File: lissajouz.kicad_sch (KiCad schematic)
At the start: 67 parts, among them J1 Conn_01x02_Male, J2 Conn_02x02_Odd_Even, Q1 2N7000, Q2 2N7000, Q3 2N7000, Q4 2N7000, Q5 2N7000, Q6 BC327, Q7 BC557, Q8 BC327, Q9 BC557, U1 LM324, U2 LM324, U3 LM324, U4 LM324, U5 TL074

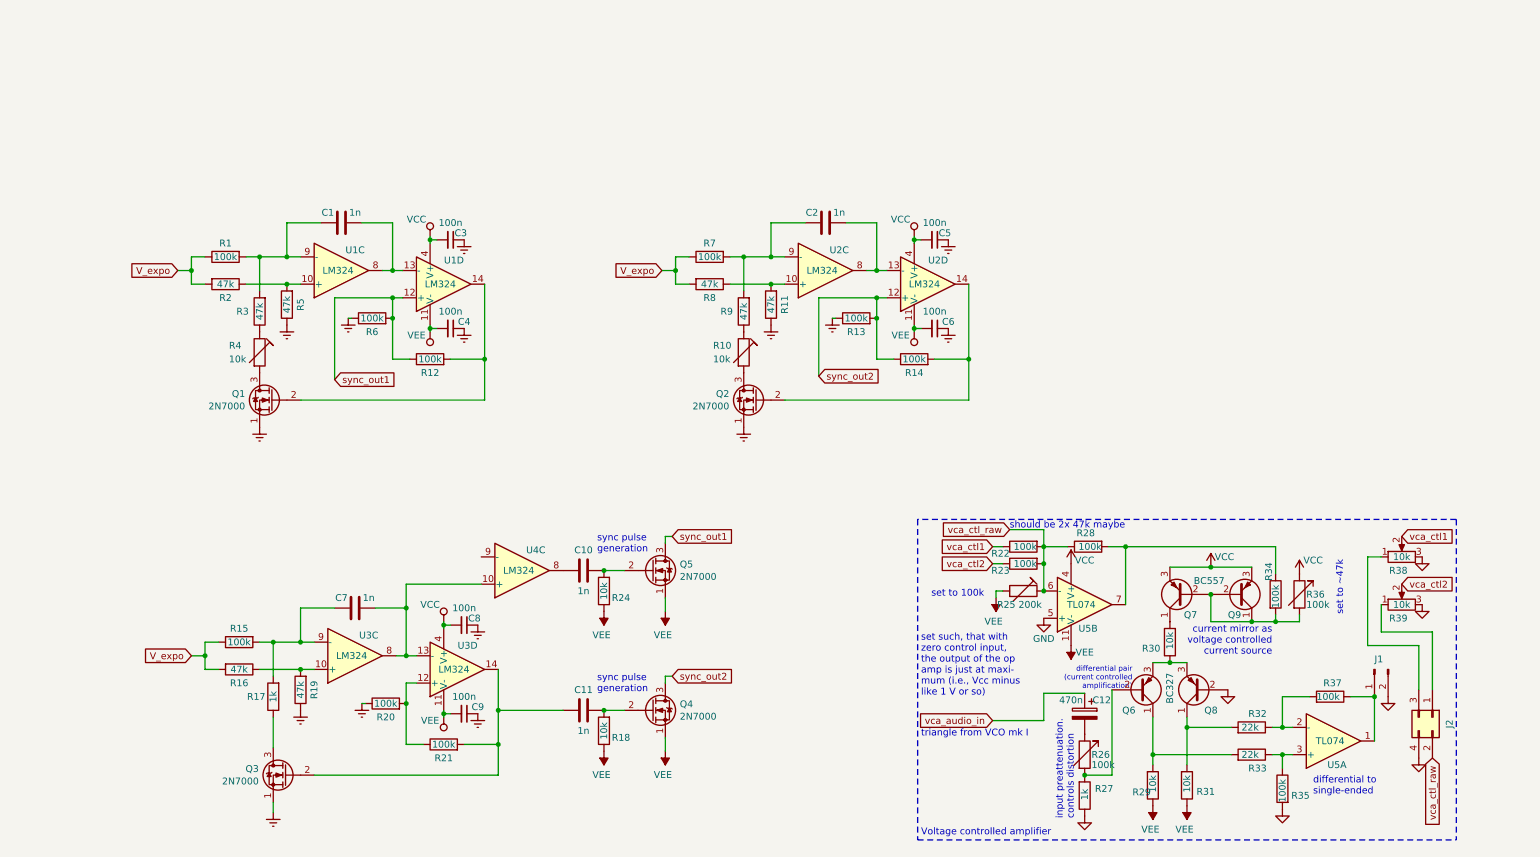
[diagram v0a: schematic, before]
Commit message: tried simulation, does not work
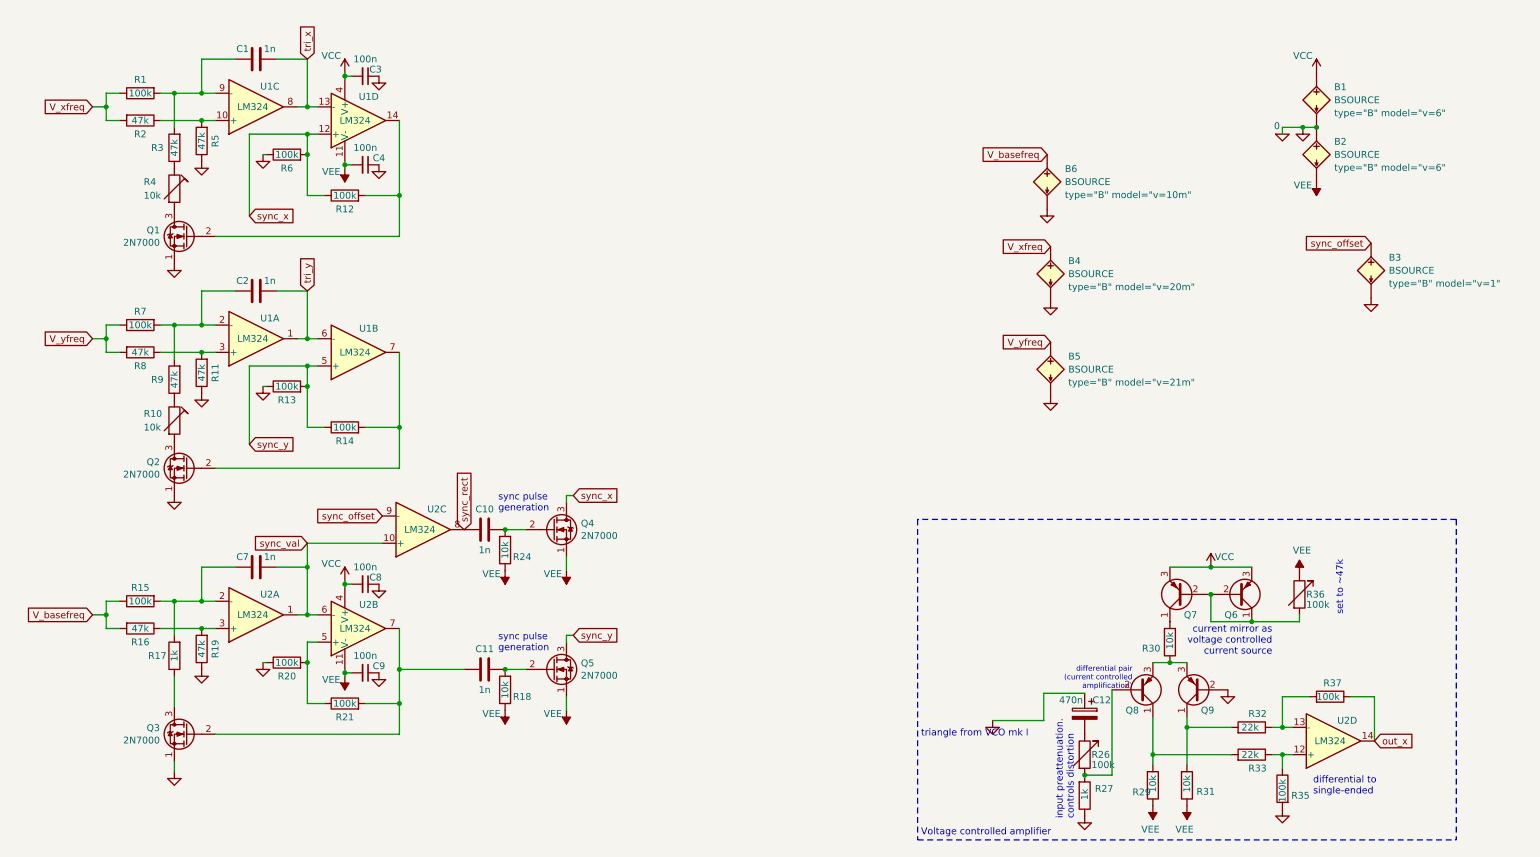
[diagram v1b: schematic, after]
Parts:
- removed C5, C6: 100n, Capacitor_SMD:C_0805_2012Metric_Pad1.15x1.40mm_HandSolder, symbol Device:C_Small
- removed J1: Conn_01x02_Male, Connector_PinHeader_2.54mm:PinHeader_1x02_P2.54mm_Vertical, symbol voice_board-rescue:Conn_01x02_Male-Connector
- removed J2: Conn_02x02_Odd_Even, Connector_PinHeader_2.54mm:PinHeader_2x02_P2.54mm_Vertical, symbol Connector_Generic:Conn_02x02_Odd_Even
- removed Q6, Q8: BC327, Package_TO_SOT_THT:TO-92_Inline, symbol Transistor_BJT:BC327
- removed R22, R23, R28, R34: 100k, Resistor_SMD:R_0805_2012Metric_Pad1.15x1.40mm_HandSolder, symbol Device:R
- removed R25: 200k, Potentiometer_THT:Potentiometer_Runtron_RM-065_Vertical, symbol voice_board-rescue:RTRIM-Device
- removed R38, R39: 10k, Potentiometer_THT:Potentiometer_Runtron_RM-065_Vertical, symbol voice_board-rescue:R_POT-Device
- removed unit 5 of U2
- removed U5: TL074, Package_DIP:DIP-14_W7.62mm, symbol Amplifier_Operational:TL074
- added B1, B2, B3, B4, B5, B6: BSOURCE, symbol Simulation_SPICE:BSOURCE
- added Q6, Q8: BC557, Package_TO_SOT_THT:TO-92_Inline, symbol Transistor_BJT:BC557
- added unit 4 of U2
- renumbered U2 to U1, U3 to U2, U4 to U2
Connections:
- net vca_audio_in is gone; now on net GND: C12.1
- net GND: now also Q9.2 (B)
- net VCC: now also B1.1 (N+), Q6.3 (E); no longer Q9.3 (E), R36.1
- net VEE: now also R36.1, B2.2 (N-)
- net at C11.1, R18.2: now also Q5.2 (G); no longer Q4.2 (G)
- net out_x: now reaches R37.1
- net out_x: now also U2.14
- net at Q7.2 (B), R36.2: now also Q6.1 (C), Q6.2 (B); no longer Q9.1 (C), Q9.2 (B)
- net at C2.2, R7.2, R9.2: now also U1.2 (-); no longer U1.9 (-)
- net at R20.2, R21.1: now also U2.5 (+); no longer U2.12 (+)
- net sync_val: now reaches C7.1, U2.10 (+)
- net sync_val: now also U2.1, U2.6 (-); no longer U2.13 (-), U2.8
- net at C11.2, Q3.2 (G), R21.2: now also U2.7; no longer U2.14
- net at R33.1, R35.1: now also U2.12 (+)
- net at R11.2, R8.1: now also U1.3 (+); no longer U1.10 (+)
- net at R29.2, R33.2: now also Q8.1 (C)
- net at R16.1, R19.2: now also U2.3 (+); no longer U2.10 (+)
- net at C7.2, R15.2, R17.2: now also U2.2 (-); no longer U2.9 (-)
- net at Q2.2 (G), R14.2: now also U1.7; no longer U1.14
- net at C10.1, R24.2: now also Q4.2 (G); no longer Q5.2 (G)
- net sync_rect: now reaches C10.2, U2.8
- net sync_offset: now reaches U2.9 (-)
- net sync_offset: now also B3.1 (N+)
- net at R26.2, R27.2: now also Q8.2 (B)
- net at R30.1: now also Q9.3 (E), Q8.3 (E)
- net at R32.1, R37.2: now also U2.13 (-)
- net at R31.2, R32.2: now also Q9.1 (C)
- net tri_x: now reaches C1.1, U1.13 (-), U1.8
- net GNDREF renamed 0
- net 0: now also B1.2 (N-), B2.1 (N+), B3.2 (N-), B4.2 (N-), B5.2 (N-), B6.2 (N-)
- removed net V_expo: R1.1, R15.1, R16.2, R2.2, R7.1, R8.2
- net sync_out1 renamed sync_x
- net sync_x: now also Q4.3 (D); no longer Q5.3 (D)
- net sync_out2 renamed sync_y
- net sync_y: now also Q5.3 (D), U1.5 (+); no longer Q4.3 (D), U1.12 (+)
- new net V_basefreq: B6.1 (N+), R15.1, R16.2
- new net V_xfreq: B4.1 (N+), R1.1, R2.2
- new net V_yfreq: B5.1 (N+), R7.1, R8.2
- new net tri_y: C2.1, U1.1, U1.6 (-)
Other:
- note removed: "set such, that with zero control input, the output of the op amp is just at maxi- mum (i.e., Vcc minus like 1 V or so)"
- note removed: "set to 100k"
- note removed: "should be 2x 47k maybe"
- moved on the sheet: C1, C10, C11, C2, C3, C4, C7, C8, C9, Q1, R1, R10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

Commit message: it wörx
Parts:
- C10: value 1n -> 10n
- Q6, Q7, Q8, Q9: symbol Transistor_BJT:BC557 -> Transistor_BJT:BC546
- R26: value 100k -> 33k
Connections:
- net GND: no longer C12.1
- net VCC: now also R29.1, R31.1, R36.1; no longer Q6.3 (E), Q7.3 (E)
- net VEE: now also Q6.3 (E), Q7.3 (E); no longer R29.1, R31.1, R36.1
- net sync_offset: now also U2.10 (+); no longer U2.9 (-)
- net sync_val: now also U2.9 (-); no longer U2.10 (+)
- net tri_x: now also C12.1
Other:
- note added: ".options gmin=1e-10 .options abstol=1e-10 .options reltol=0.005 .options cshunt=1e-15 * .options rshunt=1T"

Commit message: tuning
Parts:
- R26: value 33k -> 40k
- R3: value 47k -> 10k
- R4: value 10k -> 47k
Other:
- note added: "47k-100k"
- note removed: "set to ~47k"
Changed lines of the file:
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@@
 		)
 	)
-	(text "set to ~47k"
-		(exclude_from_sim no)
-		(at 259.08 109.855 90)
-		(effects
-			(font
-				(size 1.27 1.27)
-			)
-			(justify right bottom)
-		)
-	)
 	(text "input preattenuation.\ncontrols distortion"
 		(exclude_from_sim no)
@@
 		)
 	)
+	(text "47k-100k\n"
+		(exclude_from_sim no)
+		(at 262.255 116.84 0)
+		(effects
+			(font
+				(size 1.27 1.27)
+			)
+		)
+	)
 	(text ".options gmin=1e-10\n.options abstol=1e-10\n.options reltol=0.005\n.options cshunt=1e-15\n* .options rshunt=1T\n"
 		(exclude_from_sim no)
@@
 			)
 		)
-		(property "Value" "10k"
+		(property "Value" "47k"
 			(at 35.56 41.91 0)
 			(effects
@@
 			)
 		)
-		(property "Value" "47k"
+		(property "Value" "10k"
 			(at 41.275 33.02 90)
 			(effects
@@
 			)
 		)
+		(property "Sim.Device" "R"
+			(at 82.55 0 0)
+			(effects
+				(font
+					(size 1.27 1.27)
+				)
+				(hide yes)
+			)
+		)
+		(property "Sim.Pins" "1=+ 2=-"
+			(at 82.55 0 0)
+			(effects
+				(font
+					(size 1.27 1.27)
+				)
+				(hide yes)
+			)
+		)
 		(pin "1"
 		)
@@
 			)
 		)
-		(property "Value" "33k"
+		(property "Value" "40k"
 			(at 212.09 147.955 0)
 			(effects

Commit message: .
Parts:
- removed Q6, Q7: BC557, Package_TO_SOT_THT:TO-92_Inline, symbol Transistor_BJT:BC546
- removed R36: 100k, Potentiometer_THT:Potentiometer_Runtron_RM-065_Vertical, symbol Device:R_Variable
- added R22: 10k, Resistor_SMD:R_0805_2012Metric_Pad1.15x1.40mm_HandSolder, symbol Device:R
- C10: value 10n -> 1n
- C12: value 470n -> 100n
- R2, R5: value 47k -> 100k
- R30: value 10k -> 47k
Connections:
- net VEE: now also R30.2
- net V_xfreq: now also R22.1; no longer R1.1, R2.2
- new net: R1.1, R2.2, R22.2
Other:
- note added: "10k-110k"
- note removed: "47k-100k"
- note removed: "Voltage controlled amplifier"
- note removed: "current mirror as voltage controlled current source"
- note removed: "differential pair (current controlled amplification)"

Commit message: closer to the real thing
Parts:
- removed R10: 10k, Potentiometer_THT:Potentiometer_Bourns_3296W_Vertical, symbol vco_mk1-rescue:RTRIM-Device
- removed R4: 47k, Potentiometer_THT:Potentiometer_Bourns_3296W_Vertical, symbol vco_mk1-rescue:RTRIM-Device
- removed unit 2 of U1
- added C13, C6: 100n, Capacitor_SMD:C_0805_2012Metric_Pad1.15x1.40mm_HandSolder, symbol Device:C_Small
- added C5: 100n, Capacitor_THT:CP_Radial_D7.5mm_P2.50mm, symbol voice_board-rescue:CP-Device
- added Q6, Q7: BC557, Package_TO_SOT_THT:TO-92_Inline, symbol Transistor_BJT:BC546
- added R23: 100k, Potentiometer_THT:Potentiometer_Runtron_RM-065_Vertical, symbol Device:R_Variable
- added R25: 1k, Resistor_SMD:R_0805_2012Metric_Pad1.15x1.40mm_HandSolder, symbol Device:R
- added R28, R36: 10k, Resistor_SMD:R_0805_2012Metric_Pad1.15x1.40mm_HandSolder, symbol Device:R
- added R34: 47k, Resistor_SMD:R_0805_2012Metric_Pad1.15x1.40mm_HandSolder, symbol Device:R
- added R38, R39: 22k, Resistor_SMD:R_0805_2012Metric_Pad1.15x1.40mm_HandSolder, symbol Device:R
- added R4, R42: 47k, Potentiometer_THT:Potentiometer_Runtron_RM-065_Vertical, symbol Device:R_Variable
- added R40, R41: 100k, Resistor_SMD:R_0805_2012Metric_Pad1.15x1.40mm_HandSolder, symbol Device:R
- added unit 3 of U1
- added unit 2 of U2
- added unit 5 of U2
- R11, R8: value 47k -> 100k
- R26: value 40k -> 100k
- R9: value 47k -> 10k
- renumbered U1 to U2, U2 to U3
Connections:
- net 0: now also C13.1, C6.1
- net GND: now also Q7.2 (B), R25.1, R40.2
- net VCC: now also C6.2, R28.1, R36.1, U2.4 (V+)
- net VEE: now also C13.2, R34.2, U2.11 (V-)
- net out_x: now also R41.1, U1.8; no longer R37.1, U2.14
- net sync_x: now also U1.5 (+); no longer U1.12 (+)
- net sync_y: now also U2.5 (+)
- net tri_x: now also U1.1, U1.6 (-), C5.1; no longer C12.1, U1.13 (-), U1.8
- net tri_y: now also C12.1, U2.6 (-)
- net at R33.1, R35.1: now also U2.10 (+); no longer U2.12 (+)
- net at R3.1: now also R42.1
- net at Q1.3 (D): now also R42.2
- net at R2.1, R5.2: now also U1.3 (+); no longer U1.10 (+)
- net at Q8.1 (C), R29.2: now also R32.2; no longer R33.2
- net at Q2.2 (G), R14.2: now also U2.7
- net at C1.2, R1.2, R3.2: now also U1.2 (-); no longer U1.9 (-)
- net at R9.1: now also R4.1
- net at Q1.2 (G), R12.2: now also U1.7; no longer U1.14
- net at R32.1, R37.2: now also U2.9 (-); no longer U2.13 (-)
- net at Q2.3 (D): now also R4.2
- net at Q9.1 (C), R31.2: now also R33.2; no longer R32.2
- new net: C5.2, R23.1
- new net: Q6.2 (B), R23.2, R25.2
- new net: R39.1, R40.1, U1.10 (+)
- new net: Q6.1 (C), R28.2, R38.2
- new net: Q7.1 (C), R36.2, R39.2
- new net: Q6.3 (E), Q7.3 (E), R34.1
- new net: R38.1, R41.2, U1.9 (-)
- new net out_y: R37.1, U2.8
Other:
- note removed: "triangle from VCO mk I"
- moved on the sheet: C10, C11, C12, C7, C8, C9, Q3, Q4, Q5, Q8, Q9, R15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

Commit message: more betterer
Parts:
- added C14: 100n, Capacitor_SMD:C_0805_2012Metric_Pad1.15x1.40mm_HandSolder, symbol Device:C
- added R10, R43: 10k, Resistor_SMD:R_0805_2012Metric_Pad1.15x1.40mm_HandSolder, symbol Device:R
- added unit 4 of U1
- renumbered U3 to U2
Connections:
- net 0: no longer B3.2 (N-), B4.2 (N-), B5.2 (N-), B6.2 (N-), C13.1, C3.1, C4.1, C6.1, C8.1, C9.1, Q1.1 (S), Q2.1 (S), Q3.1 (S), R11.1, R13.1, R19.1, R20.1, R5.1, R6.1
- net VCC: now also R10.1
- net VEE: now also C14.2, R43.2
- net sync_offset: now also U2.12 (+); no longer U2.10 (+)
- net sync_rect: now also U2.14; no longer U2.8
- net sync_val: now also U2.13 (-); no longer U2.9 (-)
- new net: R10.2, R43.1, U1.12 (+)
- new net GNDREF: B3.2 (N-), B4.2 (N-), B5.2 (N-), B6.2 (N-), C13.1, C14.1, C3.1, C4.1, C6.1, C8.1, C9.1, Q1.1 (S), Q2.1 (S), Q3.1 (S), R11.1, R13.1, R19.1, R20.1, R5.1, R6.1, U1.13 (-), U1.14
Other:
- moved on the sheet: B4, B5, B6

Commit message: close to final
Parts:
- added B7: BSOURCE, symbol Simulation_SPICE:BSOURCE
- added C17: 100n, Capacitor_SMD:C_0805_2012Metric_Pad1.15x1.40mm_HandSolder, symbol Device:C
- added J1: Barrel_Jack, symbol Connector:Barrel_Jack
- added Q10: 2N7000, Package_TO_SOT_THT:TO-92_Inline, symbol Transistor_FET:2N7000
- added R44: 1Meg, Resistor_SMD:R_0805_2012Metric_Pad1.15x1.40mm_HandSolder, symbol Device:R
- added R45, R47, R48, R49, R50, R52, R54, R55, R56: 100k, Resistor_SMD:R_0805_2012Metric_Pad1.15x1.40mm_HandSolder, symbol Device:R
- added R46: 470k, Resistor_SMD:R_0805_2012Metric_Pad1.15x1.40mm_HandSolder, symbol Device:R
- added R51, R53: 10k, Resistor_SMD:R_0805_2012Metric_Pad1.15x1.40mm_HandSolder, symbol Device:R
- added R57, R58, R59: 1k, Resistor_SMD:R_0805_2012Metric_Pad1.15x1.40mm_HandSolder, symbol Device:R
- added RV1, RV10, RV2, RV3, RV4, RV5, RV6, RV7, RV8, RV9: 10k, symbol Device:R_Potentiometer
- added unit 4 of U3
- added unit 3 of U3
- B1, B2, B3, B4, B5, B6: now left out of the parts list
- R16, R19: value 47k -> 100k
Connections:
- net GNDREF: now also B7.2 (N-), Q10.1 (S), R47.1, R48.1, R57.2, RV1.3, RV10.3, RV2.3, RV3.3, RV4.3, RV5.3, RV6.3, RV7.3, RV8.3, RV9.3
- net VCC: now also J1.1, R57.1, RV5.1, RV6.1, RV7.1, RV8.1
- net VEE: now also J1.2
- net V_xfreq: now also RV5.2
- net V_yfreq: now also R51.1, RV6.2; no longer R7.1, R8.2
- net out_x: now also RV9.1
- net out_y: now also RV10.1
- net at R1.1, R2.2, R22.2: now also R50.2
- net V_basefreq: no longer names the net of R15.1, R16.2
- net V_basefreq: now also R53.2, R54.2; no longer B6.1 (N+)
- net sync_offset: no longer names the net of U2.12 (+)
- net sync_offset: now also R55.2, R56.2; no longer B3.1 (N+)
- net sync_rect: no longer names the net of C10.2, U2.14
- net sync_val renamed sync_tri
- new net: R59.2, RV10.2
- new net: R51.2, R52.2, R7.1, R8.2
- new net: R48.2, R49.1, U3.12 (+)
- new net: Q10.2 (G), R49.2, U3.14
- new net: R45.1, R47.2, U3.10 (+)
- new net: R58.2, RV9.2
- new net: C17.2, R44.2, R46.2, U3.9 (-)
- new net: Q10.3 (D), R46.1
- new net V_lfofreq: B7.1 (N+), R44.1, R45.2
- new net V_syncfreq: B6.1 (N+), R53.1, RV7.2
- new net lfo_syncfreq: R54.1, RV3.2
- new net lfo_syncphase: R56.1, RV4.2
- new net lfo_tri: C17.1, RV1.1, RV2.1, RV3.1, RV4.1, U3.13 (-), U3.8
- new net lfo_xfreq: R50.1, RV1.2
- new net lfo_yfreq: R52.1, RV2.2
- new net sync_phase: B3.1 (N+), RV8.2
- new net syncphase: R55.1
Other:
- note added: "approx 2Hz @ max 5V"
- note added: "simulates the effect of the potis which are excluded from simulation"
- moved on the sheet: B1, B2, B3, B4, B5, B6, C1, C10, C11, C12, C13, C2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

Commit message: reannotate schematic
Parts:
- renumbered B7 to B1, B6 to B2, B4 to B3, B5 to B4, B1 to B5, B2 to B6, B3 to B7, C14 to C1, C7 to C11, C8 to C12, C11 to C13, C9 to C14, C17 to C15, C5 to C2, C1 to C3, C3 to C4, C4 to C5, C12 to C6, C2 to C7, C6 to C8, C13 to C9, Q6 to Q1, Q7 to Q2, Q1 to Q3, Q8 to Q4, Q9 to Q5, Q2 to Q6, Q4 to Q7, Q5 to Q8, Q3 to Q9, R10 to R1, R2 to R10, R5 to R11, R39 to R12, R3 to R13, R6 to R14, R23 to R15, R40 to R16, R42 to R17, R12 to R18, R25 to R19, R43 to R2, R34 to R20, R29 to R21, R31 to R22, R37 to R23, R7 to R24, R51 to R25, R57 to R26, R32 to R27, R52 to R28, R8 to R29, R28 to R3, R11 to R30, R33 to R31, R9 to R32, R13 to R33, R26 to R34, R4 to R36, R14 to R37, R27 to R38, R30 to R39, R36 to R4, R55 to R40, R56 to R41, R24 to R42, R15 to R43, R53 to R44, R54 to R45, R16 to R46, R19 to R47, R17 to R48, R20 to R49, R41 to R5, R18 to R50, R21 to R51, R44 to R52, R45 to R53, R47 to R54, R46 to R55, R48 to R56, R49 to R57, R1 to R6, R22 to R7, R38 to R8, R50 to R9
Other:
- moved on the sheet: C1, C15, J1, Q10, R1, R2, R52, R53, R54, R55, R56, R57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
